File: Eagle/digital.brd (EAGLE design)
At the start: 111.1 x 72.4 mm, 23 parts, among them J1 USB-B

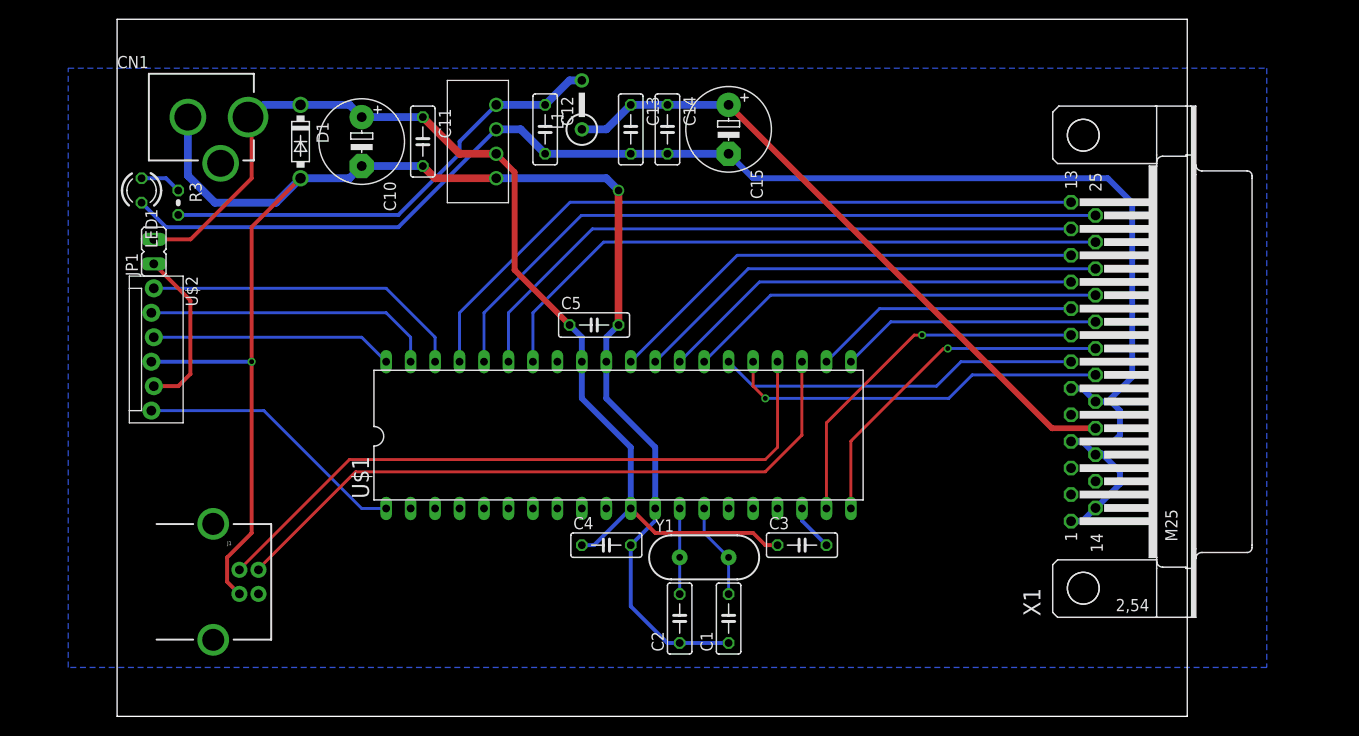
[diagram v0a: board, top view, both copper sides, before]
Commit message: Added optoisolators
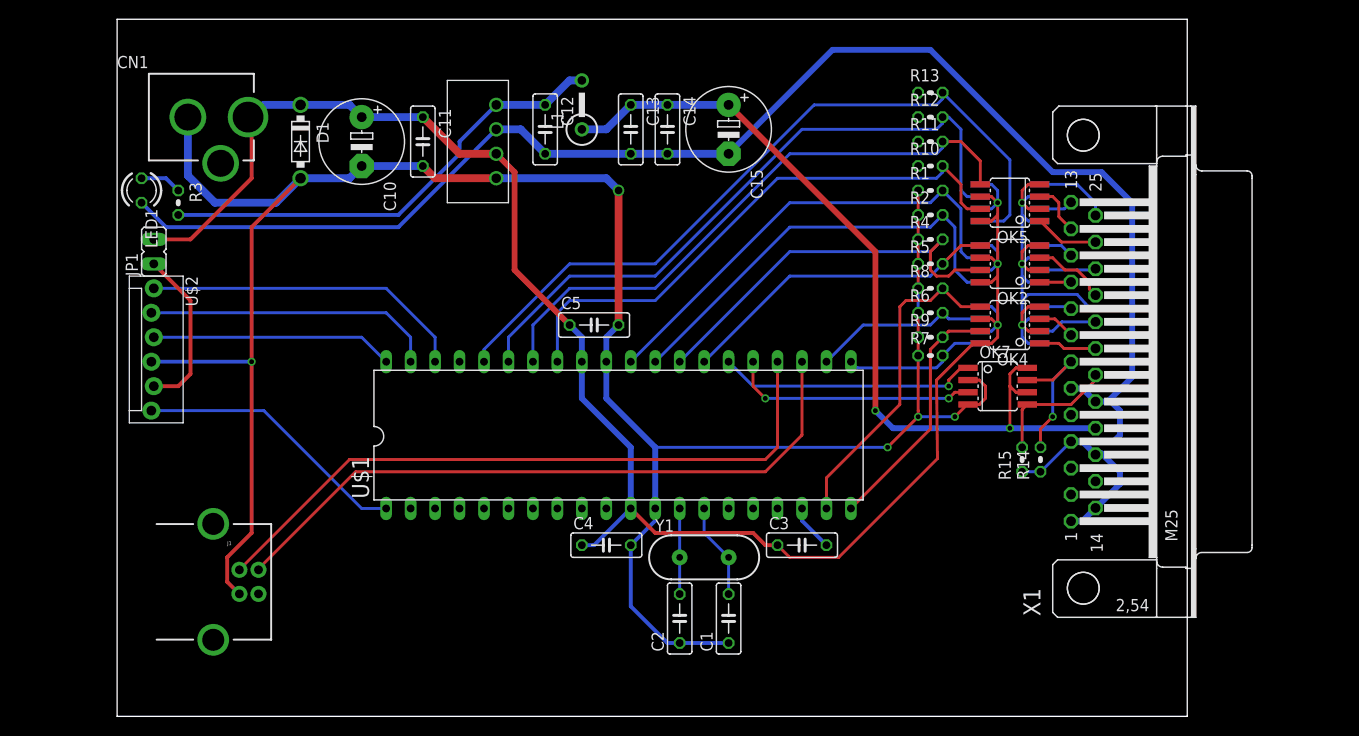
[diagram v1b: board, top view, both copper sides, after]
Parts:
- added OK1, OK2, OK3, OK4, OK5, OK6, OK7: ILD205, optocoupler:SOIC08
- added R1, R10, R11, R12, R13, R14, R15, R2, R4, R5, R6, R7, R8, R9: (no value), resistor:0204V
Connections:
- removed net CNV: U$1.25, X1.19
- removed net RD0: U$1.19, X1.8
- removed net RD1: U$1.20, X1.20
- removed net SCK: U$1.26, X1.7
- new net N$21: OK5.3, X1.12
- new net N$22: OK6.1, X1.25
- new net N$23: OK6.3, X1.13
- new net N$24: OK1.5, R2.2, U$1.29
- new net N$25: OK2.7, R4.2, U$1.28
- new net N$27: OK2.5, R5.2, U$1.27
- new net N$29: OK3.7, R6.2, U$1.22
- new net N$30: OK3.5, R7.2, U$1.21
- new net N$31: OK4.7, R9.2, U$1.20
- new net N$32: OK4.5, R8.2, U$1.19
- new net N$33: OK5.7, R10.2, U$1.33
- new net N$34: OK5.5, R11.2, U$1.34
- new net N$35: OK6.7, R12.2, U$1.35
- new net N$36: OK6.5, R13.2, U$1.36
- new net N$37: OK7.7, R14.2, X1.7
- new net N$38: OK7.5, R15.2, X1.19
- new net N$39: OK7.1, U$1.26
- new net N$40: OK7.3, U$1.25
- net +5V: now also OK7.6, OK7.8
- net +5V/2: now also OK1.6, OK1.8, OK2.6, OK2.8, OK3.6, OK3.8, OK4.6, OK4.8, OK5.6, OK5.8, OK6.6, OK6.8
- net DGND: now also OK7.2, OK7.4, R1.1, R10.1, R11.1, R12.1, R13.1, R2.1, R4.1, R5.1, R6.1, R7.1, R8.1, R9.1
- net GND: now also OK1.2, OK1.4, OK2.2, OK2.4, OK3.2, OK3.4, OK4.2, OK4.4, OK5.2, OK5.4, OK6.2, OK6.4, R14.1, R15.1
- net N$11: now also OK1.1, X1.11; no longer U$1.37, X1.13
- net N$12: now also OK1.3, X1.23; no longer U$1.36, X1.25
- net N$13: now also OK2.1, X1.10; no longer U$1.35, X1.12
- net N$14: now also OK2.3, X1.22; no longer U$1.34, X1.24
- net N$15: now also OK1.7, R1.2; no longer X1.11
- net N$16: now also OK3.1, X1.9; no longer U$1.29, X1.23
- net N$17: now also OK3.3, X1.21; no longer U$1.28, X1.10
- net N$18: now also OK4.1, X1.20; no longer U$1.27, X1.22
- net N$19: now also OK4.3, X1.8; no longer U$1.22, X1.9
- net N$20: now also OK5.1, X1.24; no longer U$1.21, X1.21
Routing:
- net N$36: track 0.00 -> 79.2 mm
- net +5V/2: track 113.8 -> 192.0 mm, vias 0 -> 3
- net GND: track 161.4 -> 231.6 mm, vias 0 -> 3
- net N$11: track 73.3 -> 3.70 mm
- net N$35: track 0.00 -> 68.5 mm
- net N$12: track 72.8 -> 5.87 mm
- net N$13: track 67.1 -> 3.29 mm
- net DGND: track 170.5 -> 233.7 mm, vias 2 -> 5
- net N$34: track 0.00 -> 61.8 mm
- net N$14: track 66.5 -> 7.84 mm
- net N$33: track 0.00 -> 58.6 mm
- net N$16: track 49.7 -> 3.36 mm
- net N$24: track 0.00 -> 45.6 mm
- net N$25: track 0.00 -> 42.0 mm
- net CNV: track 39.6 -> 0.00 mm, vias 1 -> 0
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- removed copper zone on layer 16, net GND

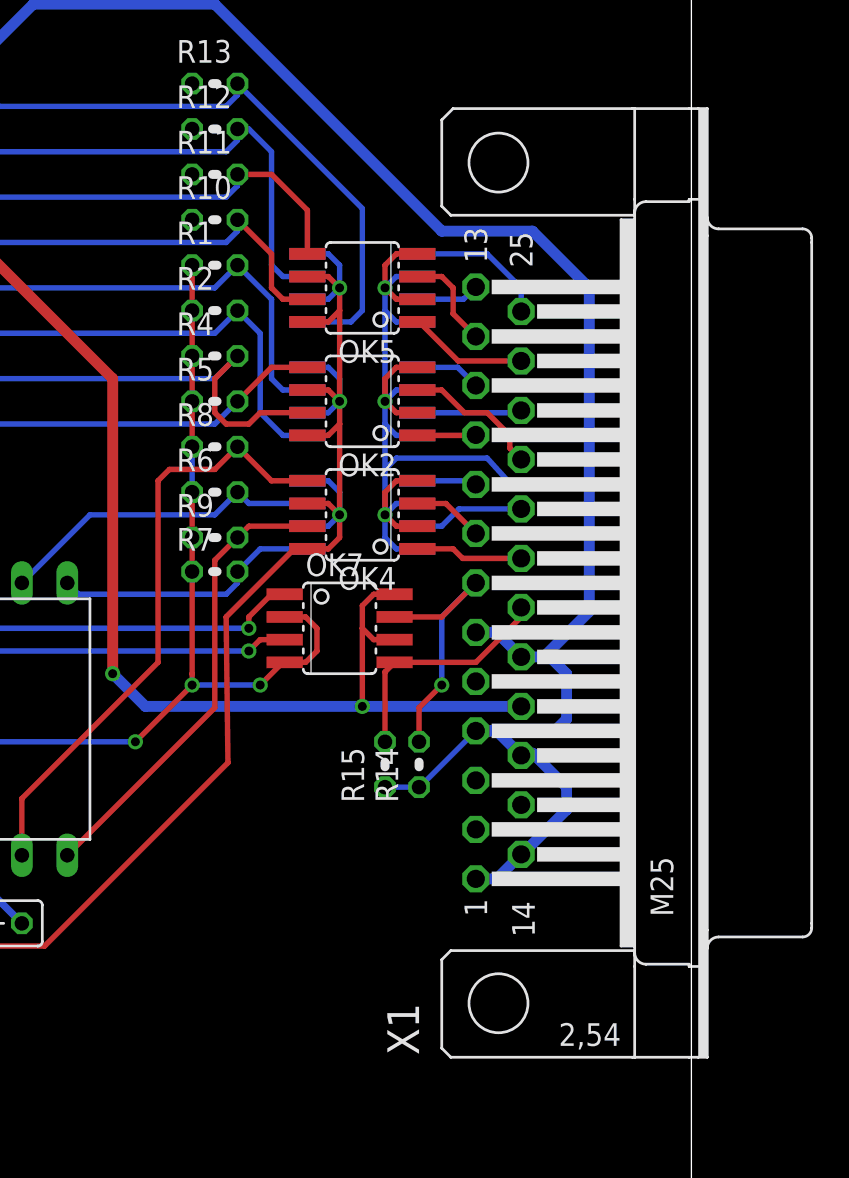
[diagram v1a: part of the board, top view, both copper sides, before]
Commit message: Corrected connector positions
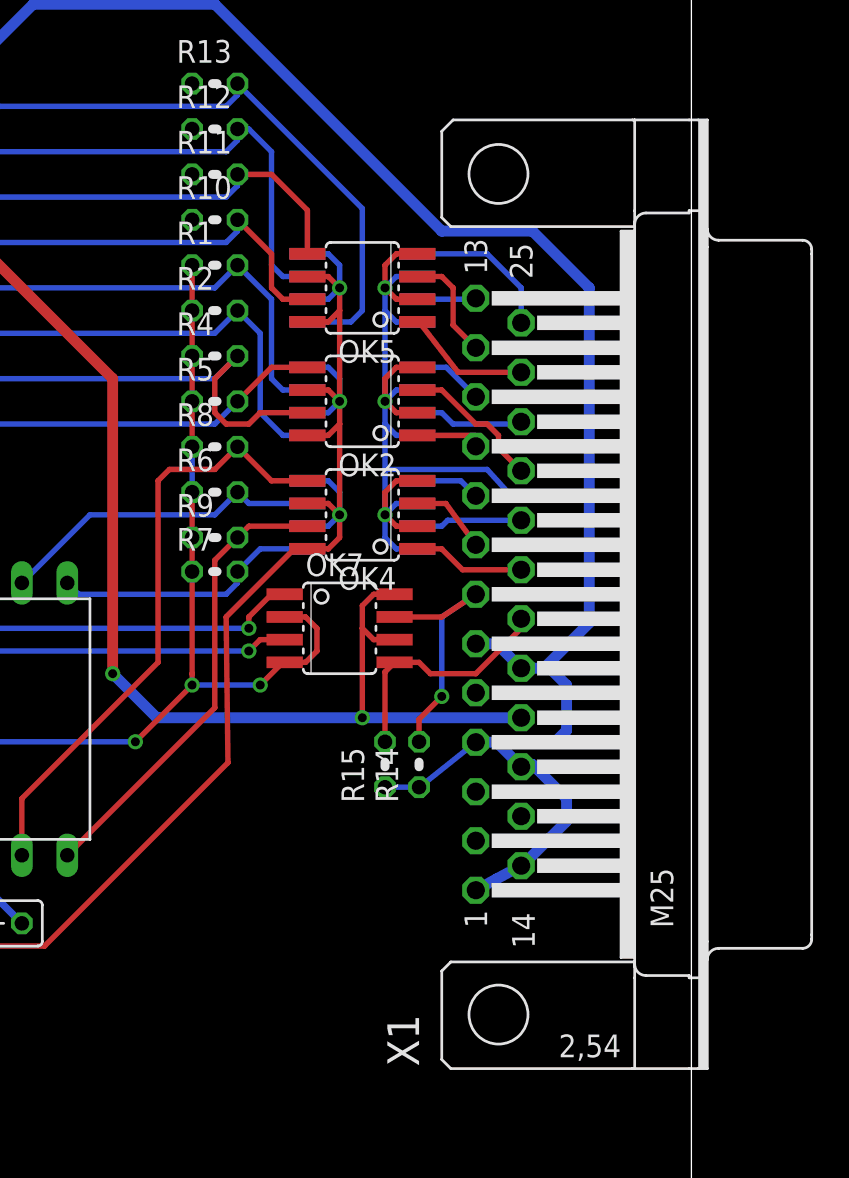
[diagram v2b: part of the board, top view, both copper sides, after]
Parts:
- moved X1 0.63 mm to (100.3, 36.2)
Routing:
- net GND: track 231.6 -> 230.1 mm
- net +5V: track 87.7 -> 88.6 mm
- net N$37: track 15.5 -> 14.7 mm
- net N$21: track 5.51 -> 6.15 mm
- net N$22: track 7.93 -> 8.56 mm
- net N$13: track 3.29 -> 3.86 mm

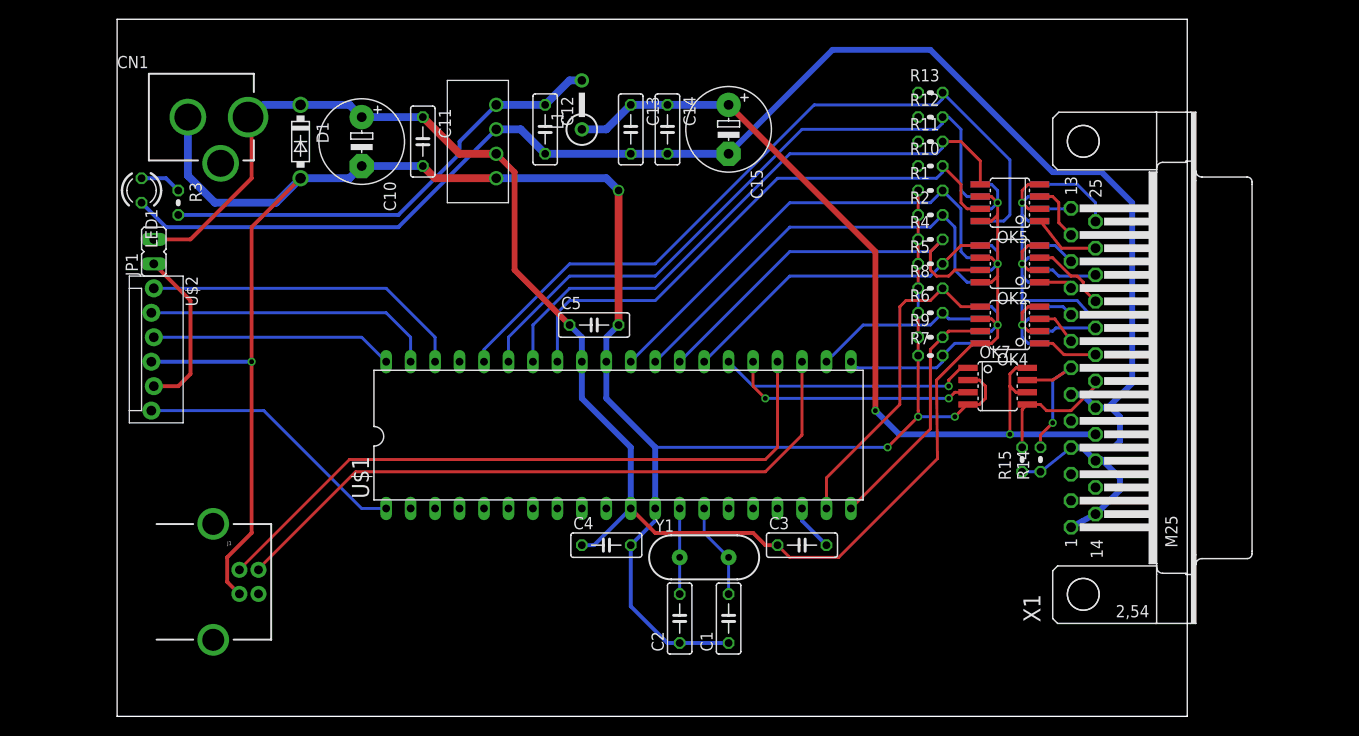
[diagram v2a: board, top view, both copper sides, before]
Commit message: Added indicator LEDs
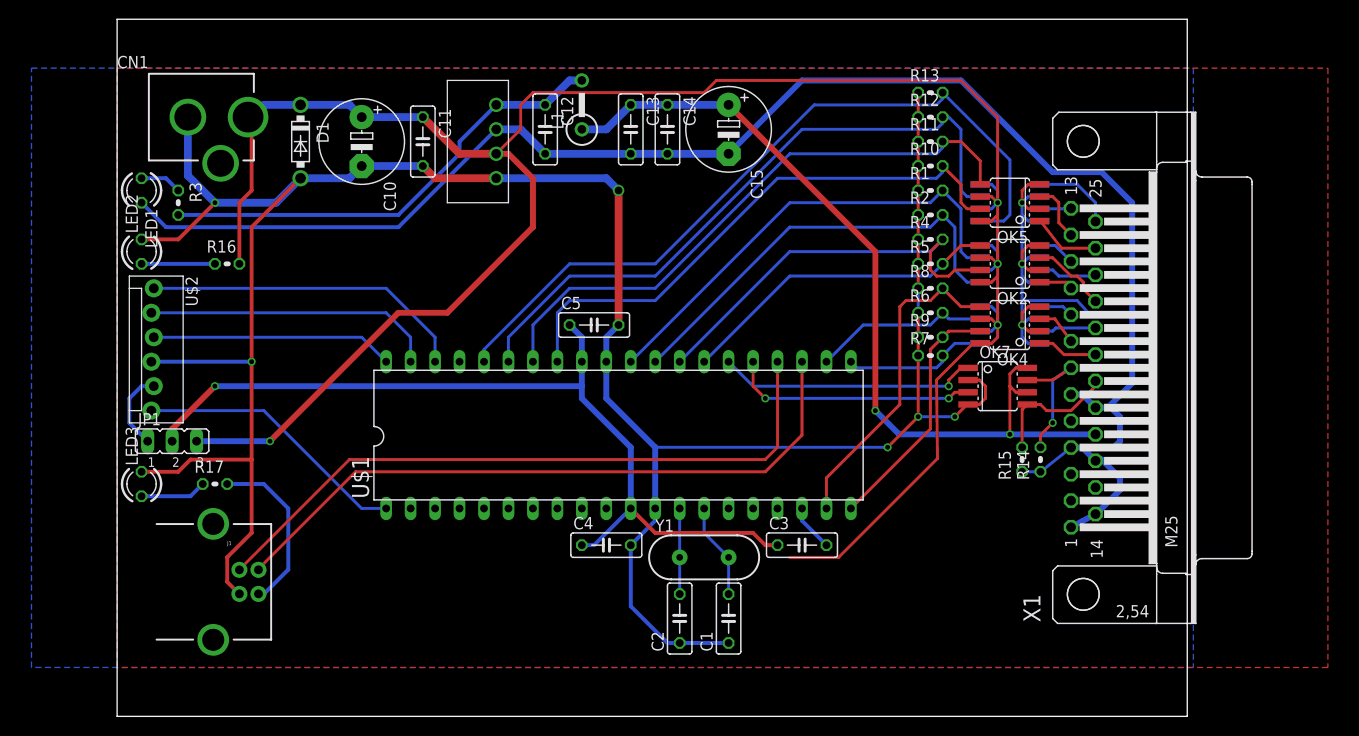
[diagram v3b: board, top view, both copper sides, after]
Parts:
- added LED2, LED3: (no value), led:LED3MM
- added R16, R17: 200k, resistor:0204V
- JP1: device jumper:JP1 -> jumper:JP2
- moved JP1 19.8 mm to (5.71, 28.6)
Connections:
- new net N$41: LED2.A, R16.1
- new net N$42: LED3.A, R17.1
- new net N$43: J1.VBUS, R17.2
- new net N$45: C3.1, C4.1, C5.1, JP1.2, U$1.11, U$1.32
- net +5V/2: now also JP1.3, R16.2; no longer C3.1, C4.1, C5.1, JP1.2, U$1.11, U$1.32
- net DGND: now also LED2.K, LED3.K
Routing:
- net N$45: track 0.00 -> 90.8 mm, vias 0 -> 1
- net +5V/2: track 192.0 -> 242.0 mm, vias 3 -> 4
- net DGND: track 233.7 -> 265.0 mm, vias 5 -> 6
- net N$43: track 0.00 -> 17.9 mm
- net N$10: track 17.3 -> 8.30 mm
- net N$41: track 0.00 -> 7.62 mm
- net N$42: track 0.00 -> 6.88 mm
- net GND: track 230.1 -> 227.5 mm
- added copper zone on layer 1, net DGND
- added copper zone on layer 16, net DGND

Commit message: Updated resistor values
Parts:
- R16, R17, R3: value 200k -> 1.65k
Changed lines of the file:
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@@
 <element name="C11" library="resistor" package="C050-025X075" value="0.1uF" x="31.75" y="59.69" rot="R270"/>
 <element name="U$3" library="modEEG" package="SIP4" value="ROL-0505S" x="38.1" y="59.69" rot="R90"/>
-<element name="R3" library="resistor" package="0204V" value="200k" x="6.35" y="53.34" rot="R270"/>
+<element name="R3" library="resistor" package="0204V" value="1.65k" x="6.35" y="53.34" rot="R270"/>
 <element name="LED1" library="led" package="LED3MM" value="" x="2.54" y="54.61" rot="R270"/>
 <element name="C12" library="resistor" package="C050-025X075" value="0.1uF" x="44.45" y="60.96" rot="R270"/>
@@
 <element name="R14" library="resistor" package="0204V" value="" x="95.885" y="26.67" rot="R90"/>
 <element name="R15" library="resistor" package="0204V" value="" x="93.98" y="26.67" rot="R90"/>
-<element name="R16" library="resistor" package="0204V" value="200k" x="11.43" y="46.99"/>
+<element name="R16" library="resistor" package="0204V" value="1.65k" x="11.43" y="46.99"/>
 <element name="LED2" library="led" package="LED3MM" value="" x="2.54" y="48.26" rot="R90"/>
-<element name="R17" library="resistor" package="0204V" value="200k" x="10.16" y="24.13"/>
+<element name="R17" library="resistor" package="0204V" value="1.65k" x="10.16" y="24.13"/>
 <element name="LED3" library="led" package="LED3MM" value="" x="2.54" y="24.13" rot="R90"/>
 <element name="JP1" library="jumper" package="JP2" value="" x="5.715" y="28.575"/>
